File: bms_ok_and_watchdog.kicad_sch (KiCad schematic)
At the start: 10 parts, among them U4 SN74LVC1G11IDCKRQ1, U5 SN74LVC1G07DCKT, U6 TPS3430WDRCR

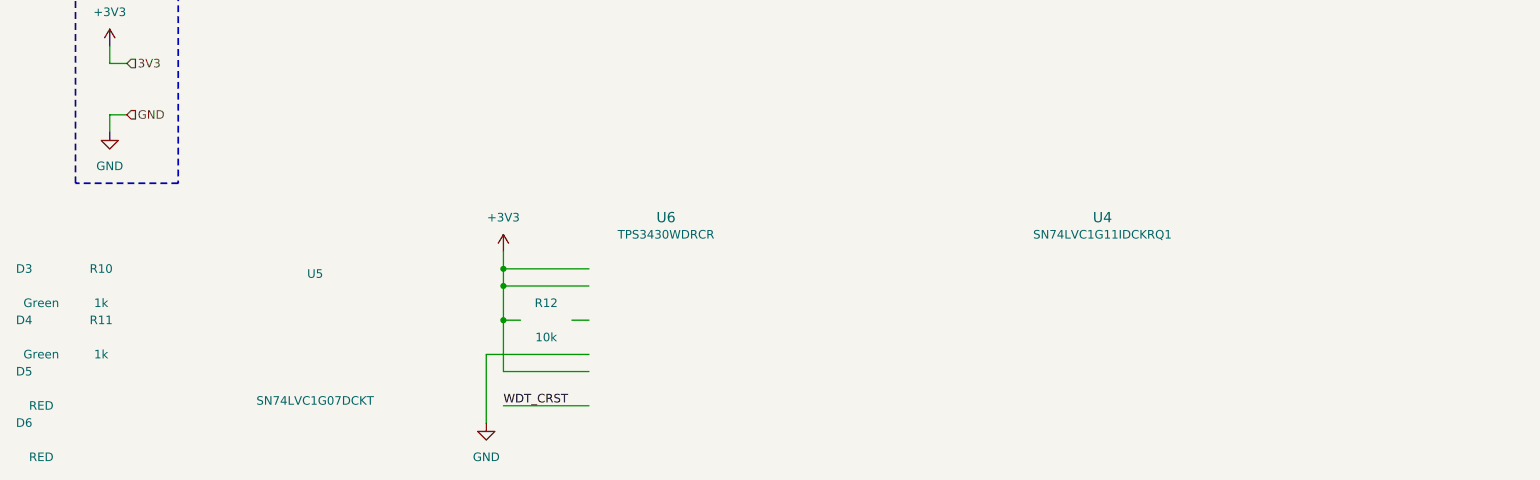
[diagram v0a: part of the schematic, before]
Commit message: SCH[Labels]: Working on pinout for tim.
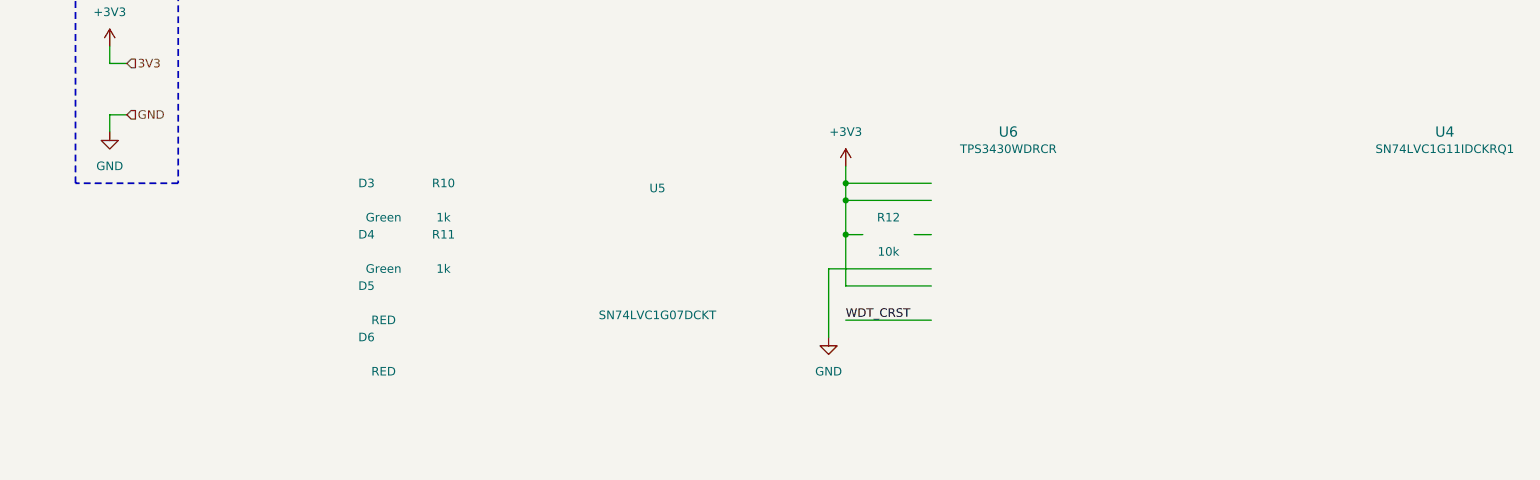
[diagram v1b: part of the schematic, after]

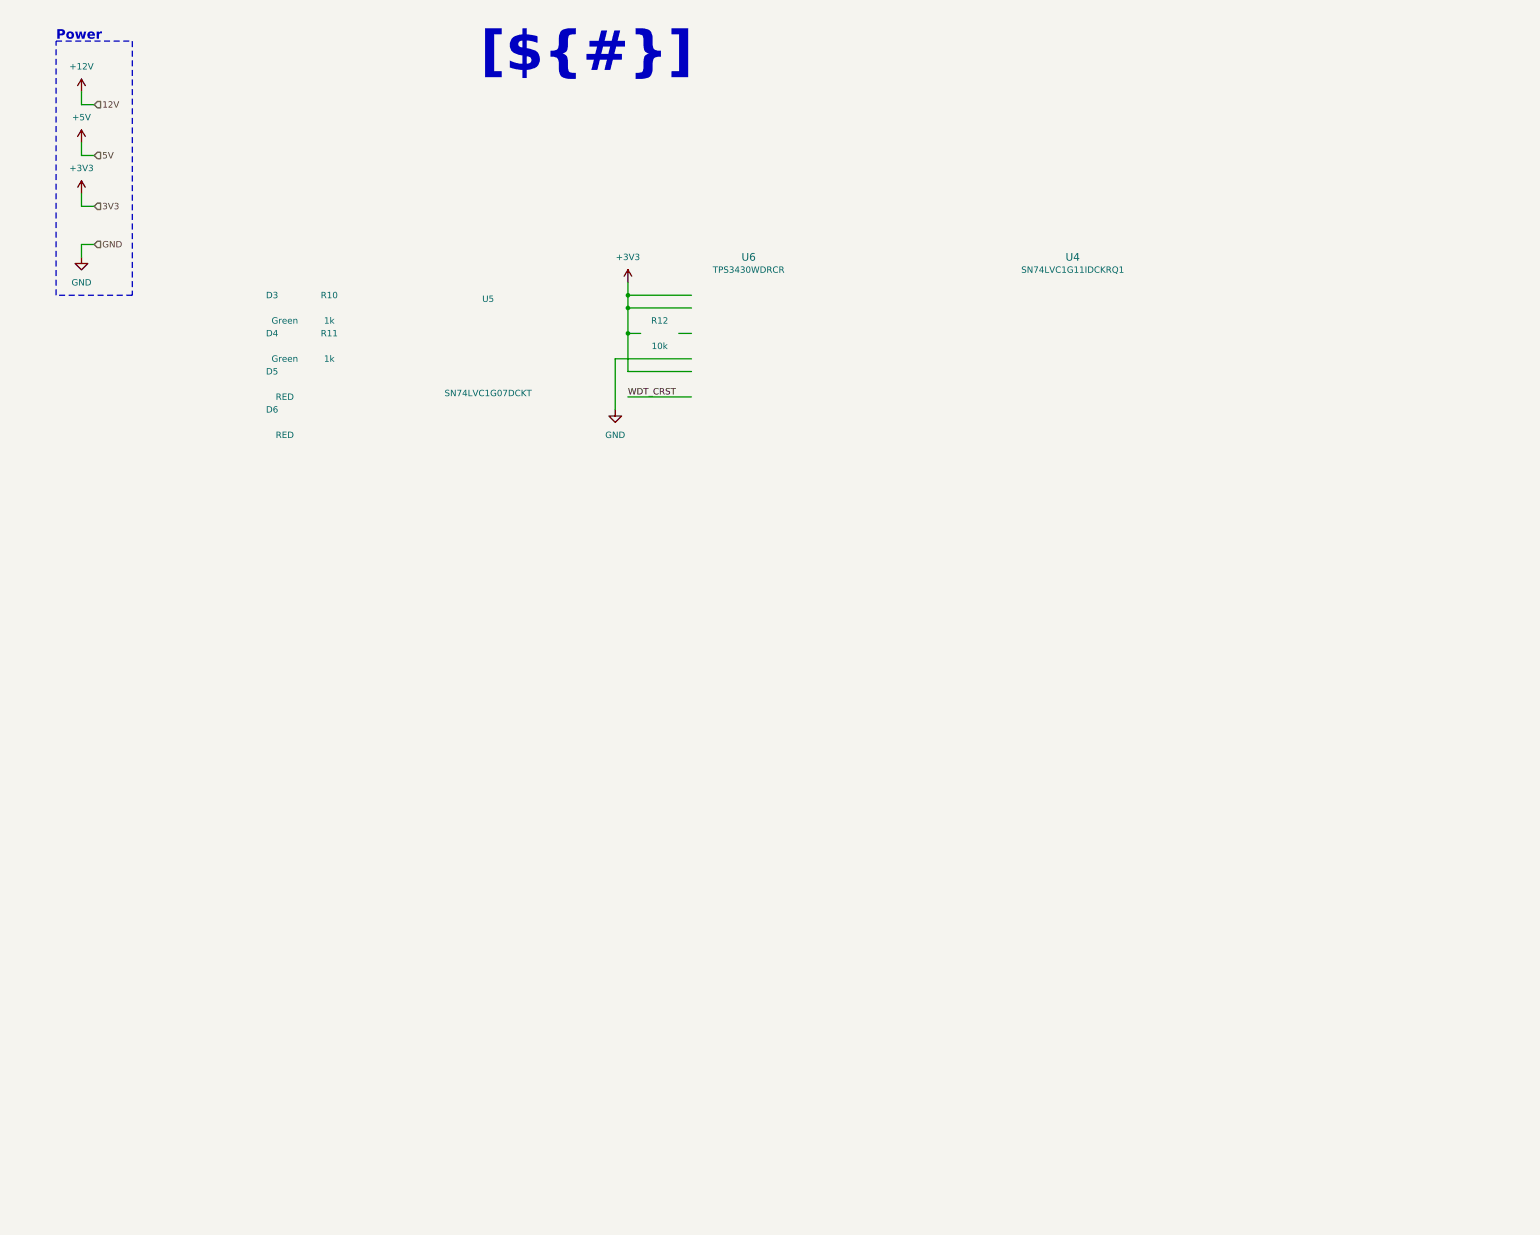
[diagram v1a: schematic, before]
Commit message: SCH[Sens & Inputs, Logic]: Started on sens and inputs condtiong, Logic page drawn. Need to add notes still.
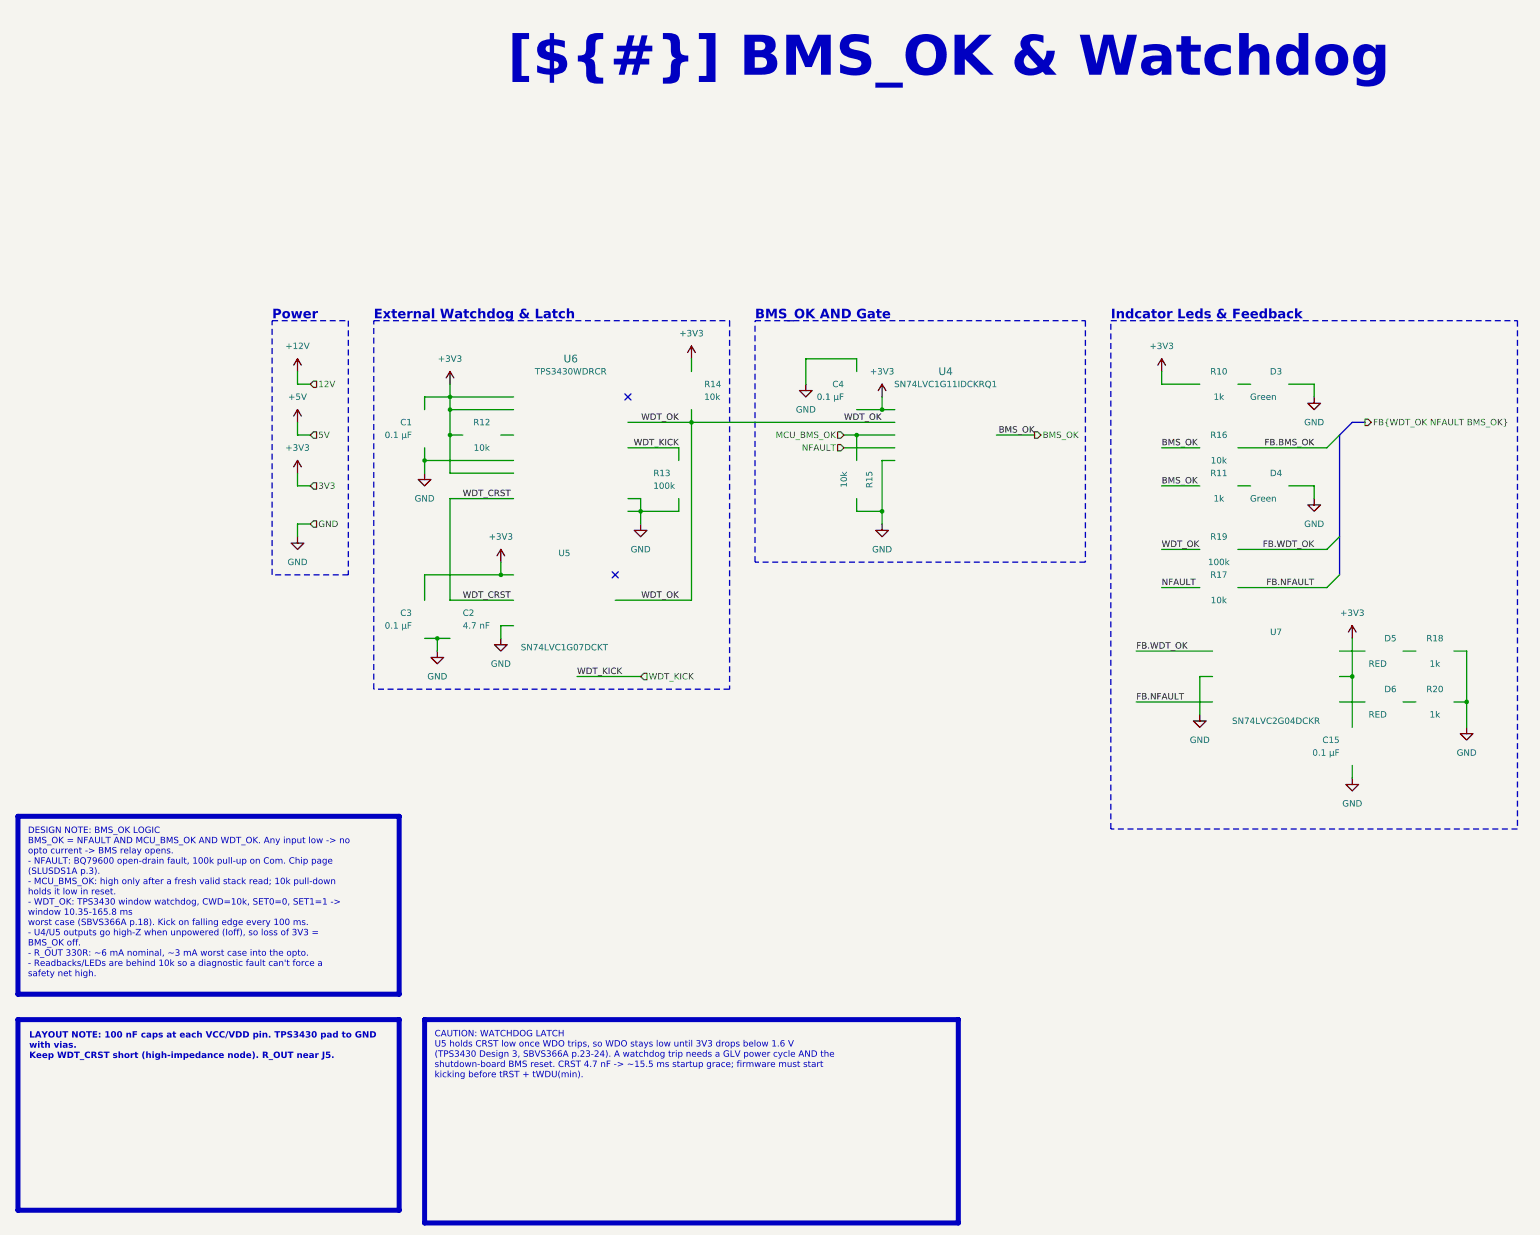
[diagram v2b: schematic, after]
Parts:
- added C1, C15, C3, C4: 0.1 µF, remote_cl05a105ko5nnnc:C_0402_1005Metric, symbol remote_gcm155r71h104ke02j:C
- added C2: 4.7 nF, remote_cga3e3x7r1h474k080ae:C_0603_1608Metric, symbol remote_grm1885c1h472ja01d:C
- added R13, R19: 100k, remote_rcs060359r0fkea:R_0603_1608Metric, symbol remote_crcw0603100kfkea:R_US
- added R14, R15, R16, R17: 10k, remote_erj-2ge0r00x:R_0402_1005Metric, symbol remote_rc0402jr-0710kl:RT0402BRD0710KL
- added R18, R20: 1k, remote_erj-2ge0r00x:R_0402_1005Metric, symbol remote_erj-2rkf1001x:R_US
- added U7: SN74LVC2G04DCKR, remote_sn74lvc2g04dckr:DCK0006A_N, symbol remote_sn74lvc2g04dckr:SN74LVC2G04DCKR
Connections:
- net +3V3: now also R10.2, U4.5 (VCC), U5.5 (VCC), C1.2, C15.2, C3.1, C4.1, R14.2, U7.5 (VCC)
- net GND: now also D3.1 (K), D4.1 (K), U4.2 (GND), U5.3 (GND), U6.11 (PAD), U6.5 (GND), C1.1, C15.1, C2.1, C3.2, C4.2, R13.1, R15.2, R18.1, R20.1, U7.2 (GND)
- net WDT_CRST: now also U5.4 (Y), C2.2
- net WDT_KICK: now reaches U6.7 (WDI)
- net WDT_KICK: now also R13.2
- net WDT_OK: now reaches U6.8 (WDO_N)
- net WDT_OK: now also U4.1 (A), U5.2 (A), R14.1, R19.1
- net MCU_BMS_OK: now reaches U4.3 (B)
- net MCU_BMS_OK: now also R15.1
- net BMS_OK: now reaches U4.4 (Y)
- net BMS_OK: now also R11.2, R16.1
- net NFAULT: now reaches U4.6 (C)
- net NFAULT: now also R17.1
- net at D6.1 (K): now also R20.2
- net at D6.2 (A): now also U7.4 (2Y)
- net at R11.1: now also D4.2 (A)
- net at D5.1 (K): now also R18.2
- net at D5.2 (A): now also U7.6 (1Y)
- net at D3.2 (A): now also R10.1
- new net FB.BMS_OK: R16.2
- new net FB.NFAULT: R17.2, U7.3 (2A)
- new net FB.WDT_OK: R19.2, U7.1 (1A)
- no-connect marks 0 -> 2
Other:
- note added: "BMS_OK AND Gate"
- note added: "External Watchdog & Latch"
- note added: "Indcator Leds & Feedback"
- title: (none) -> BMS_OK & Watchdog

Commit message: SCH[Logic, Connectors]: Removed watchdog timer going to use just stm32 interal watchdog, and com master faults. This is to simplfiy hardware less parts not needed. Adding DNP conector for halleffect sensor.
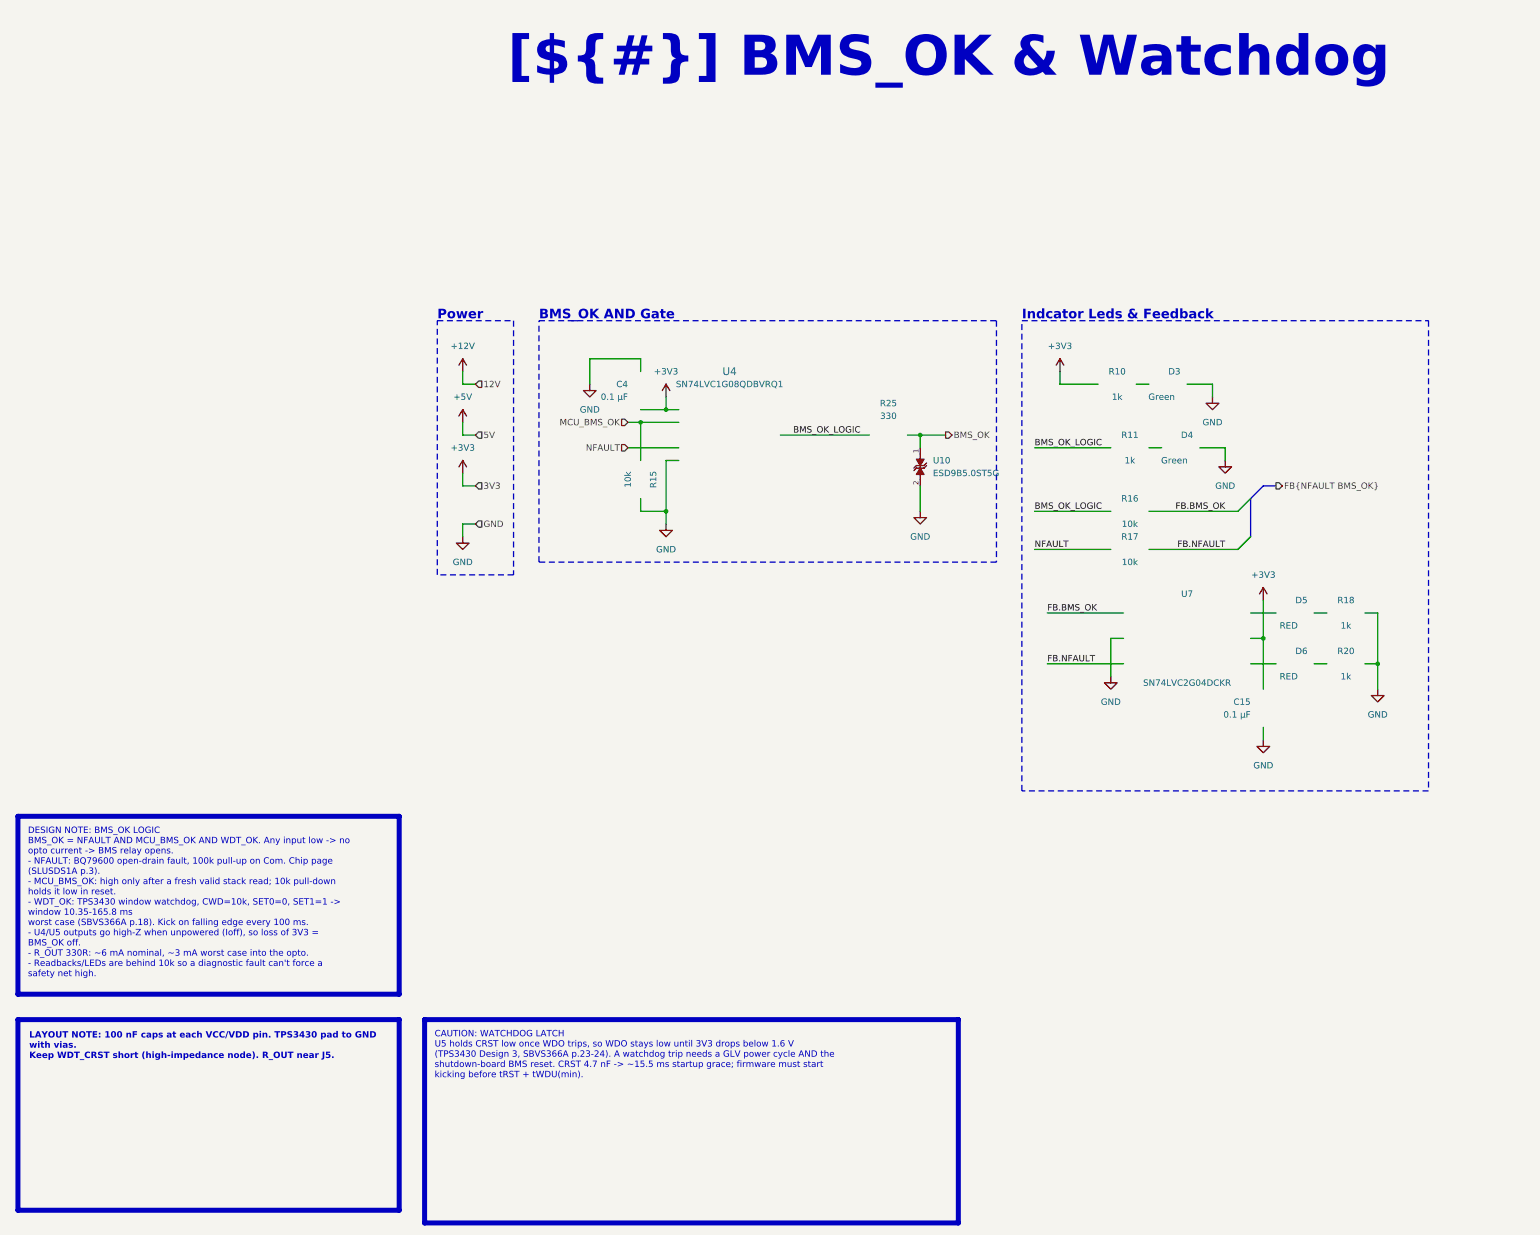
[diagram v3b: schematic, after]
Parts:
- removed C1, C3: 0.1 µF, remote_cl05a105ko5nnnc:C_0402_1005Metric, symbol remote_gcm155r71h104ke02j:C
- removed C2: 4.7 nF, remote_cga3e3x7r1h474k080ae:C_0603_1608Metric, symbol remote_grm1885c1h472ja01d:C
- removed R12, R14: 10k, remote_erj-2ge0r00x:R_0402_1005Metric, symbol remote_rc0402jr-0710kl:RT0402BRD0710KL
- removed R13, R19: 100k, remote_rcs060359r0fkea:R_0603_1608Metric, symbol remote_crcw0603100kfkea:R_US
- removed U4: SN74LVC1G11IDCKRQ1, remote_sn74lvc1g11idckrq1:DCK6, symbol remote_sn74lvc1g11idckrq1:SN74LVC1G11MDCKREP
- removed U5: SN74LVC1G07DCKT, remote_sn74lvc1g07dckt:DCK5, symbol remote_sn74lvc1g07dckt:SN74LVC1G07DCKT
- removed U6: TPS3430WDRCR, remote_tps3430wdrcr:DRC0010J_NV, symbol remote_tps3430wdrcr:TPS3430WDRCR
- added R25: 330, remote_crcw080510k0fkea:R_0805_2012Metric, symbol remote_crcw0805330rfkea:R_US
- added U10: ESD9B5.0ST5G, remote_esd9b3.3st5g:SODFL1006X40N, symbol remote_esd9b5.0st5g:ESD9B5.0ST5G
- added U4: SN74LVC1G08QDBVRQ1, remote_sn74lvc1g08qdbvrq1:DBV5, symbol remote_sn74lvc1g08qdbvrq1:SN74LVC1G08QDBVRQ1
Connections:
- net FB.WDT_OK is gone; now on net FB.BMS_OK: U7.1 (1A)
- net +3V3: now also U4.5 (VCC)
- net BMS_OK: now also R25.2, U10.1; no longer R11.2, R16.1
- net GND: now also U10.2, U4.3 (GND)
- net MCU_BMS_OK: now also U4.1 (A)
- net NFAULT: now also U4.2 (B)
- new net BMS_OK_LOGIC: R11.2, R16.1, R25.1, U4.4 (Y)
- no-connect marks 2 -> 0
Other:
- note removed: "External Watchdog & Latch"

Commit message: PCB[Daisy]: Inital layout for this.
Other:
- title: BMS_OK & Watchdog -> BMS_OK & Indicators
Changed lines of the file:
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@@
 	(paper "A3")
 	(title_block
-		(title "BMS_OK & Watchdog")
+		(title "BMS_OK & Indicators")
 		(date "2026-10-20")
 		(rev "${REVISION}")
